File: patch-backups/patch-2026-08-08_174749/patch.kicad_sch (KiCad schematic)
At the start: 45 parts, among them J1 Conn_01x03, J2 Conn_01x16, J3 Conn_Coaxial_Small, J4 Conn_01x01, J5 Conn_01x01, J6 Conn_01x01, Q1 NMOS, SW1 SW_SPST, U1 74AHC1G08, U2 W25Q12NEZPIG

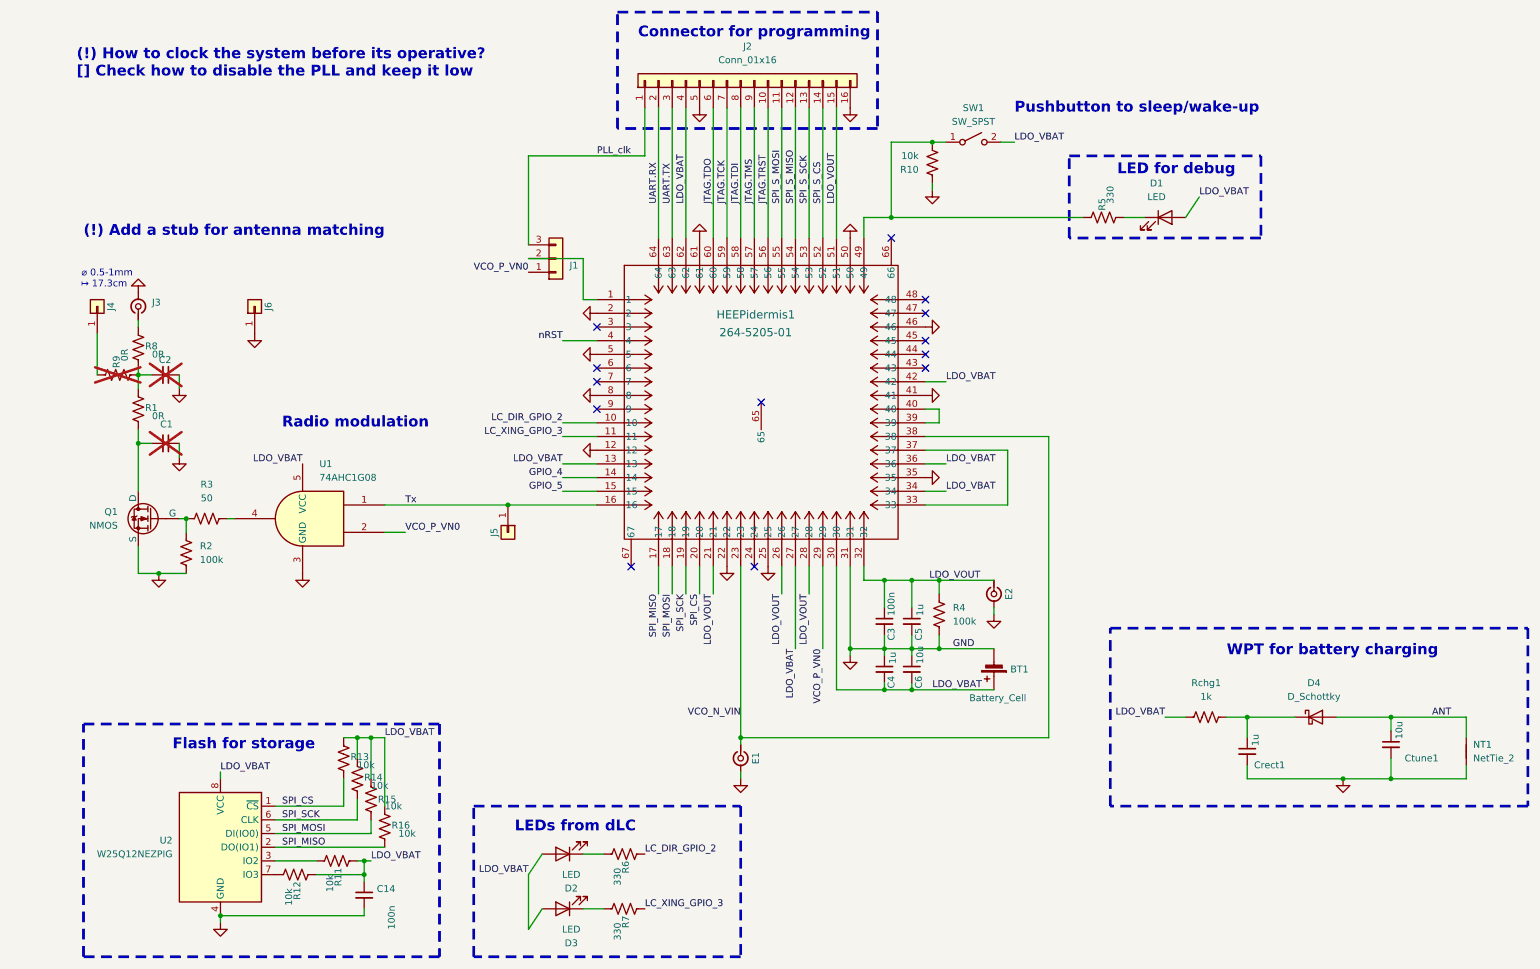
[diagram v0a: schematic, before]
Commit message: Need to fix rst, ldo vbat and check parity
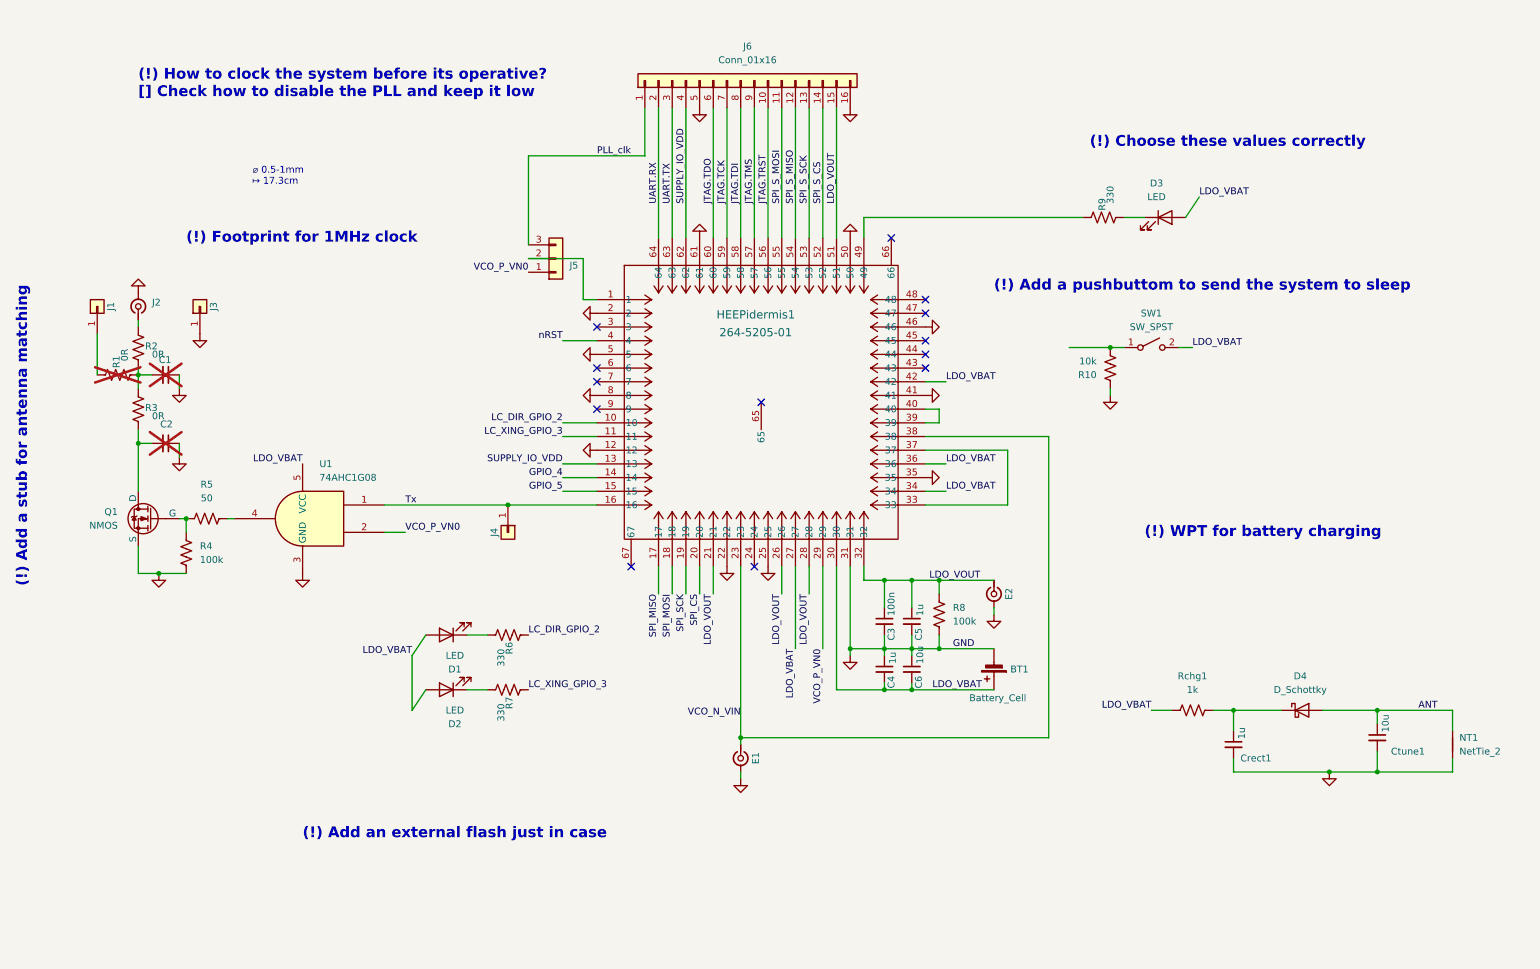
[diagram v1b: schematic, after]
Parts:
- removed C14: 100n, Capacitor_SMD:C_0603_1608Metric, symbol Device:C_Small
- removed R11, R12, R13, R14, R15, R16: 10k, Resistor_SMD:R_0603_1608Metric, symbol Device:R_US
- removed U2: W25Q12NEZPIG, Package_SO:SOIC-8_5.23x5.23mm_P1.27mm, symbol Memory_Flash:W25Q16JVSS
- SW1: footprint libs:SPST_1.6x3mm -> Button_Switch_SMD:SW_SPST_FSMSM
- renumbered C2 to C1, C1 to C2, D2 to D1, D3 to D2, D1 to D3, J4 to J1, J3 to J2, J6 to J3, J5 to J4, J1 to J5, J2 to J6, R9 to R1, R8 to R2, R1 to R3, R2 to R4, R3 to R5, R4 to R8, R5 to R9
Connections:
- net LDO_VBAT: no longer HEEPidermis1.13, HEEPidermis1.62, J6.4 (Pin_4)
- net at HEEPidermis1.49, R9.2: no longer R10.1, SW1.1 (A)
- new net: R10.1, SW1.1 (A)
- new net SUPPLY_IO_VDD: HEEPidermis1.13, HEEPidermis1.62, J6.4 (Pin_4)
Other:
- note added: "(!) Add a pushbuttom to send the system to sleep"
- note added: "(!) Add an external flash just in case"
- note added: "(!) Choose these values correctly"
- note added: "(!) Footprint for 1MHz clock"
- note added: "(!) WPT for battery charging"
- note removed: "Connector for programming"
- note removed: "Flash for storage"
- note removed: "LED for debug"
- note removed: "LEDs from dLC"
- note removed: "Pushbutton to sleep/wake-up"
- note removed: "Radio modulation"
- note removed: "WPT for battery charging"
- moved on the sheet: D1, D2, J3, R6, R7
